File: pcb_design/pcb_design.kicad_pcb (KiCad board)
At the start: 2 copper layers, 90 x 40 mm, 5 parts, among them SW1 SW_Push, SW2 SW_Push, SW3 SW_Push, U1 MOUDLE-SEEEDUINO-XIAO, U2 ER_OLEDM0.91_1x-I2C

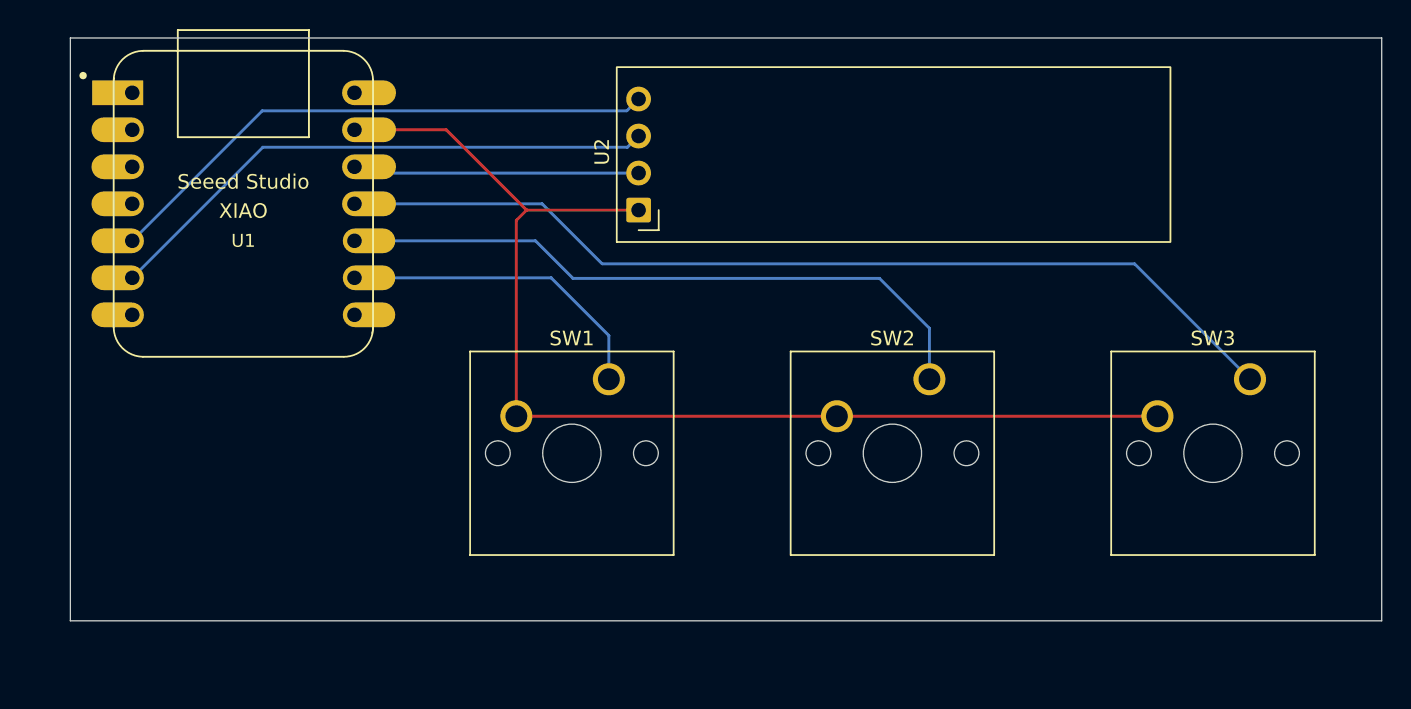
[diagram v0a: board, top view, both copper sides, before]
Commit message: Update PCB design files with layout adjustments and new STEP file
- Changed default plot path in `pcb_design.kicad_pro` to "./".
- Added new wire connections in `pcb_design.kicad_sch` for improved circuit layout.
- Reorganized existing wire connections and updated UUIDs for consistency.
- Adjusted symbol positions and properties for switches in `pcb_design.kicad_sch`.
- Introduced a new STEP file for 3D modeling of the PCB design.
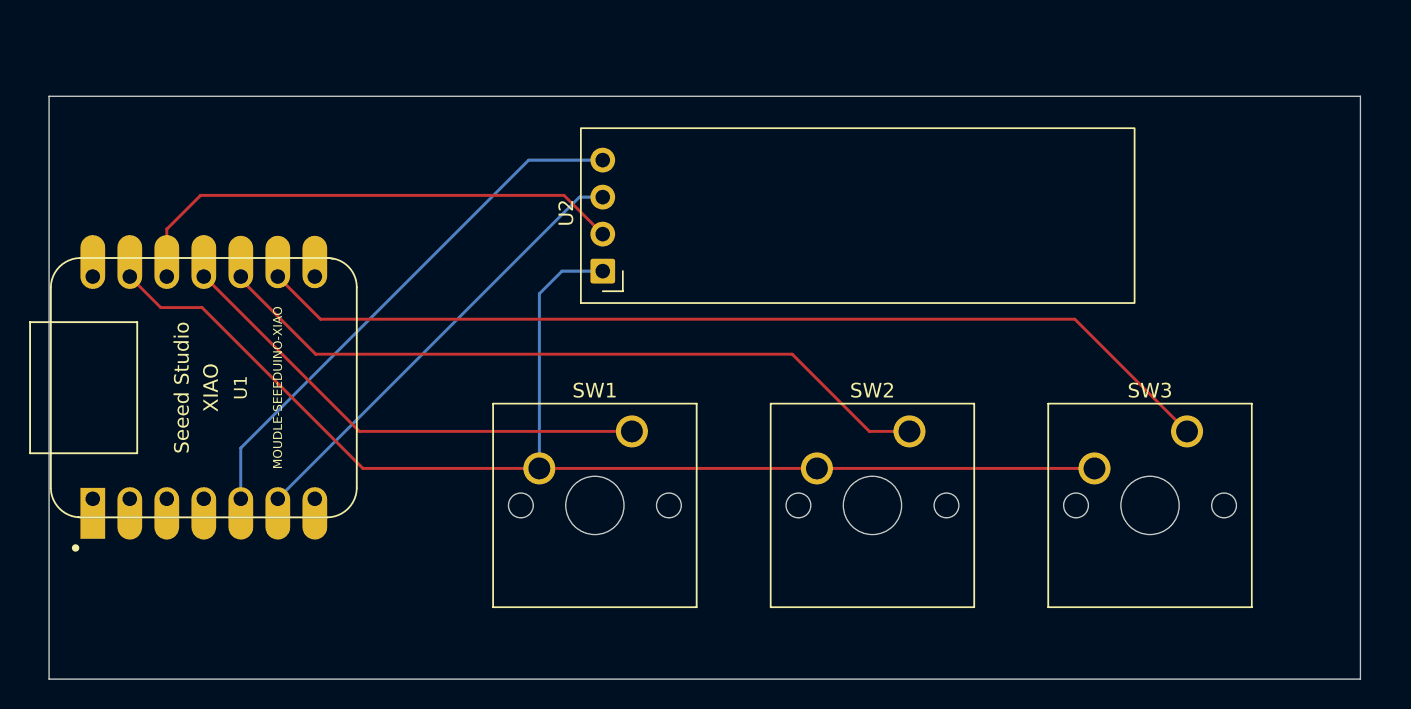
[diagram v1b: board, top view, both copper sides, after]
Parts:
- moved U1 12.9 mm to (120.6, 110.0), turned to 90 degrees
- moved SW3 5.61 mm to (188.1, 113.0)
- moved U2 4.86 mm to (148.0, 102.0)
- moved SW1 3.91 mm to (150.0, 113.0)
- moved SW2 3.83 mm to (169.1, 113.0)
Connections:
- SW1 pad 1: Net-(U1-PA7_A8_D8_SCK) -> Net-(U1-PA6_A10_D10_MOSI)
- SW3 pad 1: Net-(U1-PA6_A10_D10_MOSI) -> Net-(U1-PA7_A8_D8_SCK)
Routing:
- net Net-(U1-PA7_A8_D8_SCK): track 22.1 -> 66.8 mm
- net Net-(U1-PA6_A10_D10_MOSI): track 66.4 -> 33.8 mm
- net Net-(U1-3V3): track 19.7 -> 35.2 mm
- net GND: track 80.2 -> 88.6 mm
- net Net-(U1-PA9_A5_D5_SCL): track 38.8 -> 30.9 mm
- net Net-(U1-PA5_A9_D9_MISO): track 45.4 -> 50.4 mm
- net Net-(U1-PA8_A4_D4_SDA): track 38.8 -> 36.5 mm
